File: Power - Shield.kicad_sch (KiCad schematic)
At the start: 24 parts

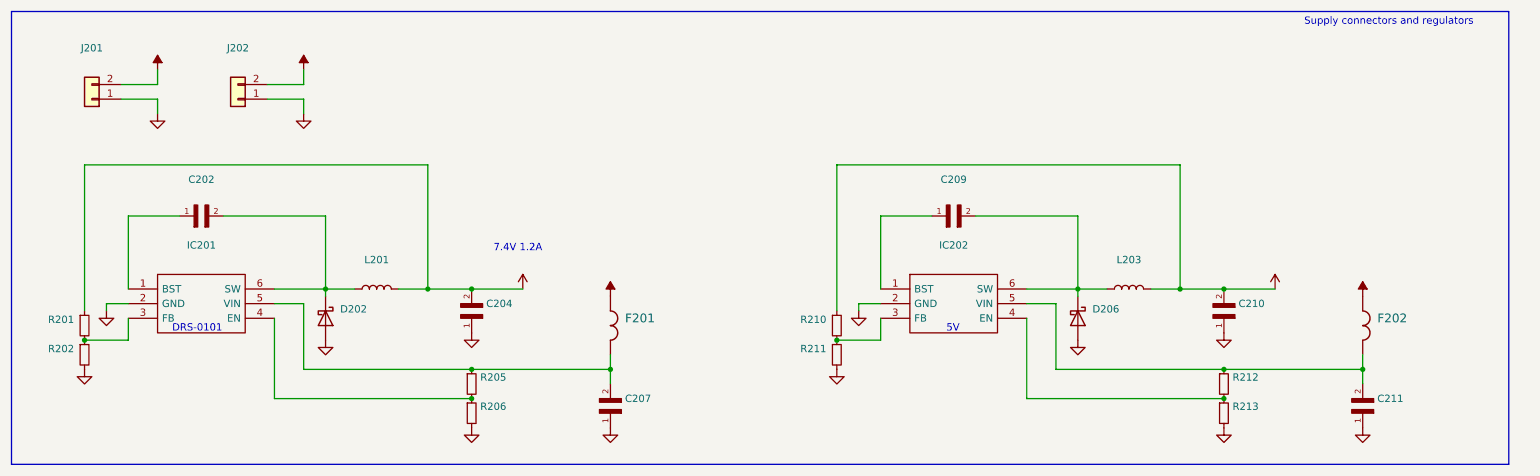
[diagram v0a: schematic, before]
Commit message: incorporated rework into official design
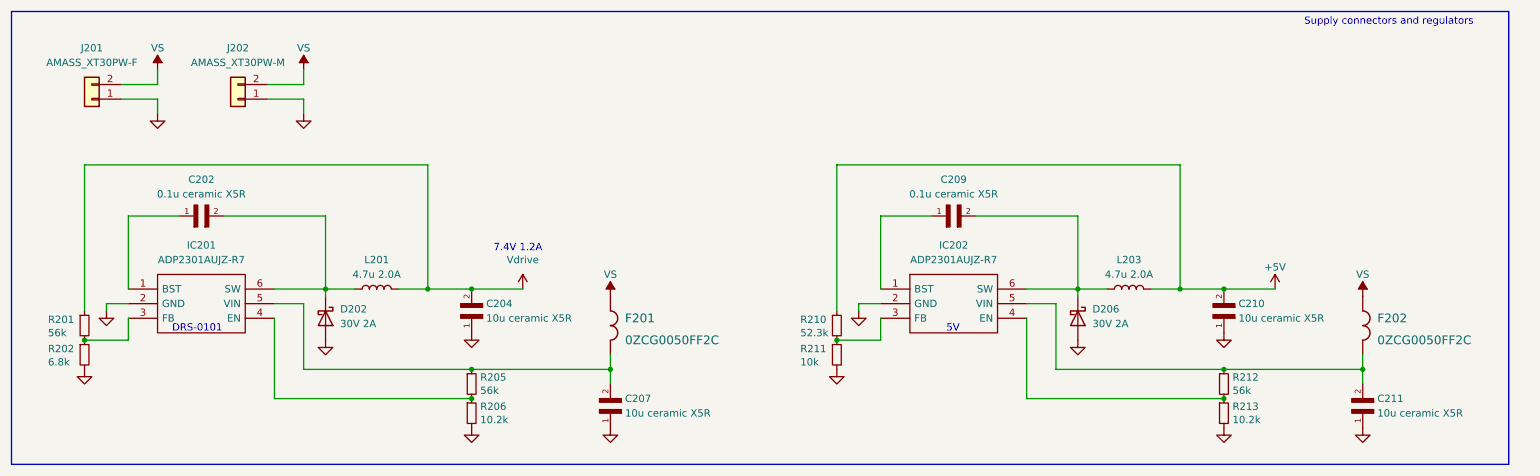
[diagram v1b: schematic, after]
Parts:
- C202, C209: value (none) -> 0.1u ceramic X5R; footprint (none) -> SnapEDA Library:CAPC1005X55N
- C204, C207, C210, C211: value (none) -> 10u ceramic X5R; footprint (none) -> SnapEDA Library:CAPC1608X90N
- D202, D206: value (none) -> 30V 2A; footprint (none) -> SnapEDA Library:B230A-13-F
- F201, F202: value (none) -> 0ZCG0050FF2C; footprint (none) -> SnapEDA Library:0ZCG0050FF2C
- IC201, IC202: value (none) -> ADP2301AUJZ-R7; footprint (none) -> SOT95P280X100-6N
- J201: value (none) -> AMASS_XT30PW-F; footprint (none) -> Connector_AMASS:AMASS_XT30PW-F_1x02_P2.50mm_Horizontal
- J202: value (none) -> AMASS_XT30PW-M; footprint (none) -> Connector_AMASS:AMASS_XT30PW-M_1x02_P2.50mm_Horizontal
- L201, L203: value (none) -> 4.7u 2.0A; footprint (none) -> SnapEDA Library:CDRH5D28RHPNP-4R7NC
- R201, R205, R212: value (none) -> 56k; footprint (none) -> Resistor_SMD:R_0402_1005Metric
- R202: value (none) -> 6.8k; footprint (none) -> Resistor_SMD:R_0402_1005Metric
- R206, R213: value (none) -> 10.2k; footprint (none) -> Resistor_SMD:R_0402_1005Metric
- R210: value (none) -> 52.3k; footprint (none) -> Resistor_SMD:R_0402_1005Metric
- R211: value (none) -> 10k; footprint (none) -> Resistor_SMD:R_0402_1005Metric
